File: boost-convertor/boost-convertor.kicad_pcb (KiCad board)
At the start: 2 copper layers, 35 parts, among them J2 Screw_Terminal_01x02, J3 AVR-ISP-6, J4 TYPE-C 6P, U1 ATMEGA328P-AU, U2 MC34063ECN, U3 ADS1115IDGSR, U4 MAX7219, Y1 Crystal

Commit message: complete layout
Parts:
- J3: footprint footprint:AVR-4pin -> footprint:AVR-5pin
- L1: value 68uH -> 100uH
- R4: value 120k -> 146.7k
- R5: value 25k -> 16.7k
- U4: footprint footprint:TQFP32_32A_MCH -> footprint:SSOP-24
- moved J2 84.9 mm to (135.9, 66.2), turned to 90 degrees
- moved RV1 71.1 mm to (123.2, 53.5), turned to 0 degrees
- moved U2 63.7 mm to (127.1, 58.2), turned to 90 degrees
- moved L1 59.7 mm to (112.0, 62.2), turned to -90 degrees
- moved RCS1 56.0 mm to (111.2, 52.0)
- moved R12 54.5 mm to (99.3, 62.5), turned to -90 degrees
- moved D1 53.8 mm to (114.0, 69.5), turned to 180 degrees
- moved R13 49.3 mm to (104.0, 67.4), turned to 90 degrees
- moved R11 49.2 mm to (104.0, 62.5), turned to -90 degrees
- moved R9 47.2 mm to (98.8, 76.5), turned to 180 degrees
- moved R4 46.7 mm to (115.2, 55.2)
- moved D2 44.7 mm to (106.8, 74.4)
- moved R2 44.6 mm to (111.2, 55.2)
- moved R5 43.2 mm to (115.2, 52.0)
- moved J4 43.1 mm to (91.3, 65.5), turned to -90 degrees
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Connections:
- C1 pad 2: PGND -> GND
- C2 pad 2: SGND -> GND
- C3 pad 2: PGND -> GND
- J2 pad 2: PGND -> GND
- R3 pad 1: SGND -> GND
- U2 pad 2: PGND -> GND
- U2 pad 4: PGND -> GND
- U3 pad 1: SGND -> GND
- U3 pad 3: SGND -> GND
- U4 pad 4: PGND -> GND
- U4 pad 9: PGND -> GND
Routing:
- net +5V: track 0.00 -> 76.6 mm, vias 0 -> 9
- net /BOOST_OUTPUT: track 0.00 -> 71.2 mm
- net GND: track 0.00 -> 70.4 mm, vias 0 -> 14
- net /SCK: track 0.00 -> 50.1 mm, vias 0 -> 2
- net Net-(LED1-f): track 0.00 -> 47.9 mm, vias 0 -> 1
- net /MOSI: track 0.00 -> 35.0 mm, vias 0 -> 2
- net Net-(LED1-e): track 0.00 -> 34.8 mm, vias 0 -> 2
- net Net-(LED1-a): track 0.00 -> 33.8 mm
- net Net-(LED1-b): track 0.00 -> 31.9 mm
- net Net-(LED1-c): track 0.00 -> 30.0 mm
- net /RESET: track 0.00 -> 29.1 mm, vias 0 -> 1
- net Net-(LED1-d): track 0.00 -> 28.0 mm
- net Net-(U1-PC5(ADC5/SCL/PCINT13)): track 0.00 -> 26.9 mm, vias 0 -> 3
- net Net-(LED1-g): track 0.00 -> 26.8 mm, vias 0 -> 2
- net Net-(U2-CII): track 0.00 -> 26.3 mm, vias 0 -> 1
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- added copper zone on In2.Cu, net +5V
- added copper zone on In1.Cu, net GND
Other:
- board outline added: 54.1 x 60.3 mm
- copper layers 2 -> 4

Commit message: The finnal pcb complete
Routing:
- net Net-(LED1-f): track 47.9 -> 20.2 mm
- net Net-(LED1-G4): track 10.4 -> 31.9 mm
- net Net-(LED1-g): track 26.8 -> 46.1 mm, vias 2 -> 0
- net Net-(LED1-a): track 33.8 -> 21.5 mm, vias 0 -> 1
- net Net-(LED1-e): track 34.8 -> 25.6 mm, vias 2 -> 0
- net Net-(LED1-b): track 31.9 -> 23.0 mm, vias 0 -> 1
- net Net-(LED1-d): track 28.0 -> 22.0 mm
- net Net-(LED1-dp): track 21.5 -> 27.2 mm, vias 2 -> 1
- net Net-(LED1-G1): track 12.0 -> 7.27 mm, vias 2 -> 0
- net Net-(U4-ISET): track 7.34 -> 8.84 mm
- net Net-(U2-IPK): track 19.9 -> 21.3 mm
- net /SS: track 25.2 -> 24.2 mm
- net Net-(LED1-G3): track 12.8 -> 13.7 mm
- net Net-(LED1-G2): track 15.4 -> 15.0 mm, vias 0 -> 2
- net Net-(LED1-c): track 30.0 -> 30.1 mm, vias 0 -> 1
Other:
- board text added: "boost convertor V1.0 made by ZhouYc"

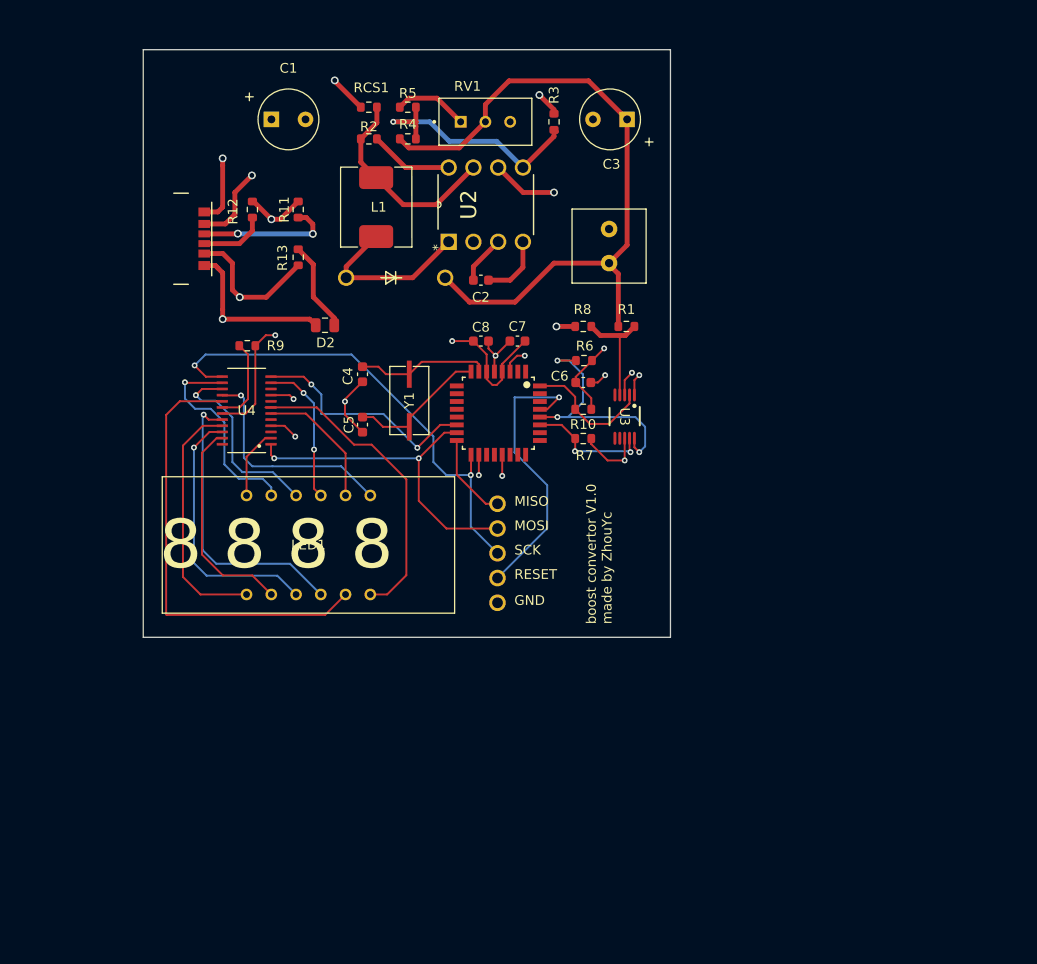
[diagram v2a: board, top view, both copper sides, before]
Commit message: add a external mosfet improve ouput power
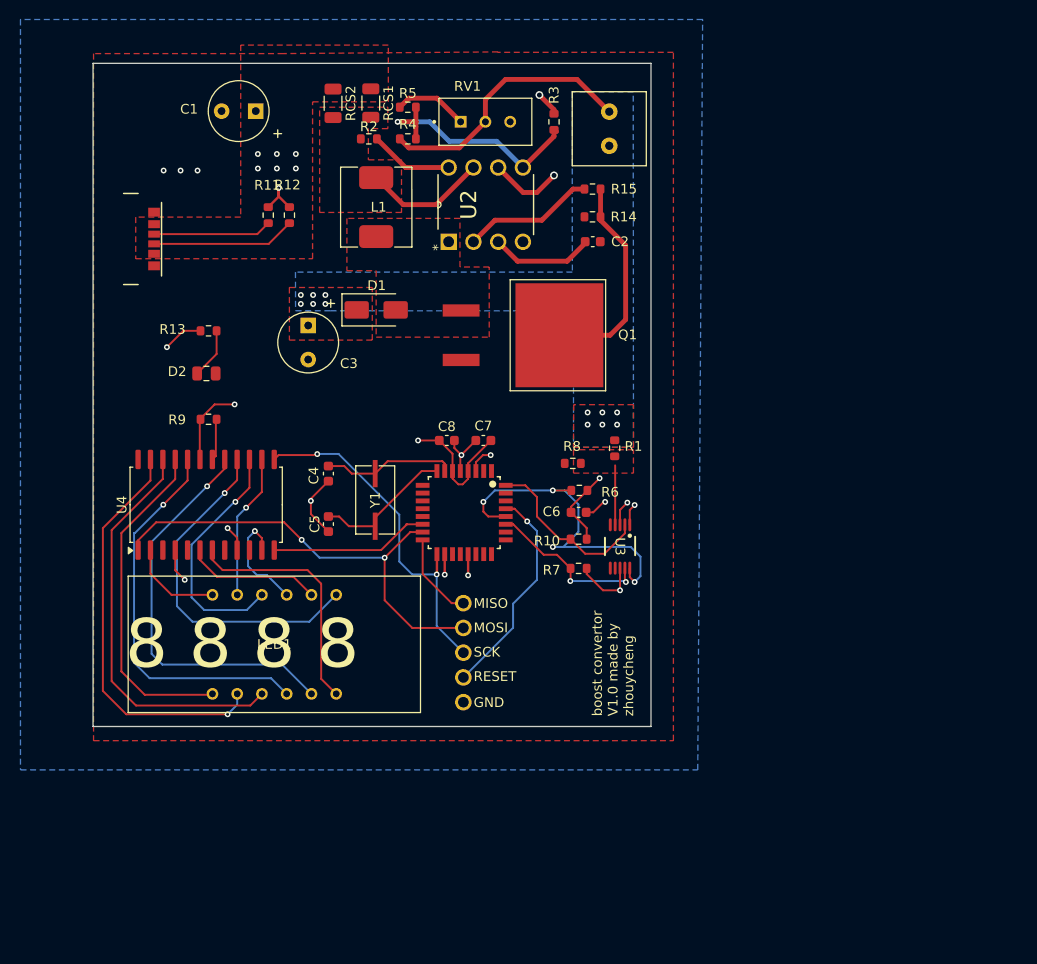
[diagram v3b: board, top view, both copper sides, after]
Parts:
- added Q1: IRL540NSPBF, footprint:TO254P1524X483-3N, F.Cu at (126.5, 75.4)
- added R14: 10k, Resistor_SMD:R_0603_1608Metric, F.Cu at (134.2, 63.2)
- added R15: 100, Resistor_SMD:R_0603_1608Metric, F.Cu at (134.2, 60.4)
- added RCS2: 0.1 1w, Resistor_SMD:R_1206_3216Metric, F.Cu at (107.6, 51.6)
- C4, C5: value 0.1u -> 18pf
- D1: value 1N5819 -> IN5819; footprint footprint:DO41-10 -> Diode_SMD:D_SMA
- RCS1: value 0.225 -> 0.1 1w; footprint Resistor_SMD:R_0603_1608Metric -> Resistor_SMD:R_1206_3216Metric
- U4: footprint footprint:SSOP-24 -> Package_SO:SOP-24_7.5x15.4mm_P1.27mm
- moved C3 39.0 mm to (105.0, 74.4), turned to -90 degrees
- moved R8 14.1 mm to (132.2, 88.5)
- moved C6 13.3 mm to (132.8, 93.6)
- moved R10 13.3 mm to (132.8, 96.3)
- moved R6 13.3 mm to (132.8, 91.3)
- moved R7 13.3 mm to (132.8, 99.3)
- moved U3 13.3 mm to (137.0, 97.1)
- moved D2 13.1 mm to (94.6, 79.3), turned to 180 degrees
- moved R1 12.6 mm to (136.5, 87.0), turned to -90 degrees
- moved C2 12.1 mm to (134.2, 65.8)
- moved J2 12.0 mm to (135.9, 54.2), turned to -90 degrees
- moved R13 11.9 mm to (94.8, 75.0), turned to 0 degrees
- moved C5 10.8 mm to (107.1, 94.8)
- moved C7 10.8 mm to (123.0, 86.2)
- moved C8 10.8 mm to (119.2, 86.2)
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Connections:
- net Net-(U2-IPK) renamed /L_IN
- net Net-(U3-AIN0) renamed /sample
- L1 pad 2: Net-(U2-SWC) -> /L_OUT
- U2 pad 1: Net-(U2-SWC) -> /L_OUT
- U2 pad 2: GND -> Net-(U2-SWE)
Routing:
- net /BOOST_OUTPUT: track 71.2 -> 27.5 mm, vias 0 -> 12
- net GND: track 70.4 -> 37.8 mm
- net +5V: track 76.8 -> 51.1 mm, vias 9 -> 13
- net Net-(Q1-G): track 0.00 -> 21.9 mm
- net Net-(LED1-d): track 22.0 -> 42.1 mm, vias 0 -> 1
- net Net-(U2-SWC): track 17.5 -> 0.00 mm
- net Net-(LED1-dp): track 27.2 -> 41.9 mm, vias 1 -> 0
- net /SCK: track 50.1 -> 36.1 mm
- net Net-(U2-SWE): track 0.00 -> 13.6 mm
- net Net-(LED1-b): track 23.0 -> 35.8 mm
- net /MOSI: track 35.0 -> 47.2 mm
- net Net-(LED1-c): track 30.1 -> 40.2 mm
- net Net-(U1-PC5(ADC5/SCL/PCINT13)): track 26.9 -> 36.2 mm, vias 3 -> 4
- net Net-(LED1-e): track 25.6 -> 34.4 mm
- net /L_IN: track 21.3 -> 12.7 mm
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- added copper zone on F.Cu, net +5V
- added copper zone on B.Cu, net /BOOST_OUTPUT
- added copper zone on F.Cu, net /BOOST_OUTPUT
- added copper zone on F.Cu, net /L_IN
- added copper zone on F.Cu, net /L_OUT
- added copper zone on F.Cu, net /sample
- added copper zone on B.Cu, net GND
- added copper zone on F.Cu, net GND
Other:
- board size 54.1 x 60.3 mm -> 57.2 x 68 mm
- board text added: "boost convertor V1.0 made by zhouycheng"
- board text removed: "boost convertor V1.0 made by ZhouYc"

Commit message: correct drc
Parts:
- moved R6 10.7 mm to (132.9, 102.0)
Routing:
- net Net-(U1-PC5(ADC5/SCL/PCINT13)): track 36.2 -> 26.1 mm, vias 4 -> 2
- net +5V: track 51.1 -> 52.0 mm, vias 13 -> 14
- net GND: vias 14 -> 17

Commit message: update v1.1
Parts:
- added G***: LOGO, footprint:flower, B.Cu at (96.4, 76.2)
- added G***: LOGO, footprint:fox_skillscreen, B.Cu at (125.6, 81.6)
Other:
- board text added: "Ctd. ZhouYC"
- board text added: "boost convertor V1.0"
- board text added: "言葉は 風にのりで 心を結ぶ かなのまい 筆先に咲く 音の花 静寂にも 日本語のひ 優しく照らす"
- board text removed: "boost convertor V1.0 made by zhouycheng"
